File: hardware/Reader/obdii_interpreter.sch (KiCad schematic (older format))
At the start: 0 parts

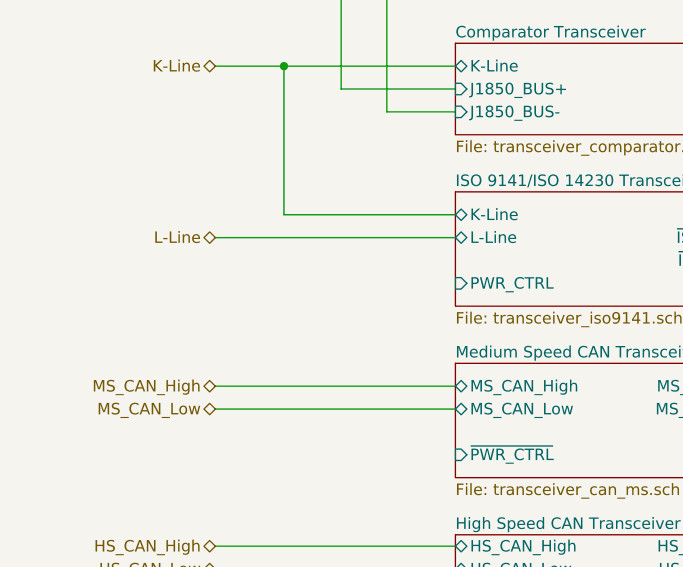
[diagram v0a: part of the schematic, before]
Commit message: Completed Reader schematics for version 0.0.01
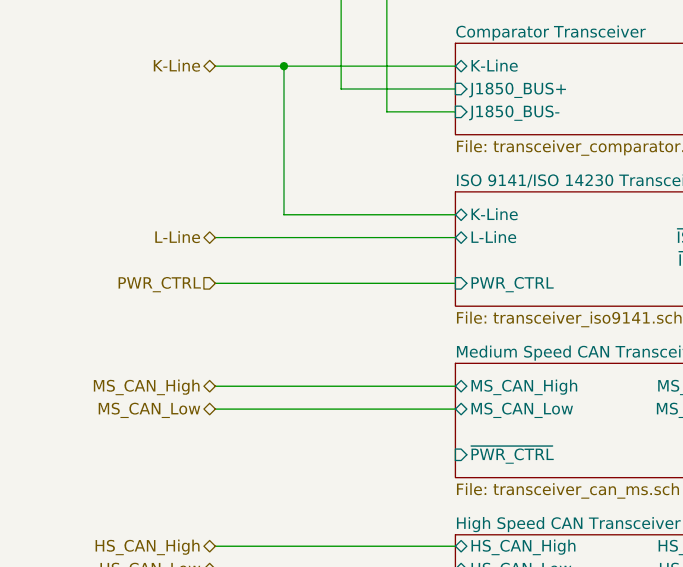
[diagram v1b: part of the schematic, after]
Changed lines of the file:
@@
 $Descr USLetter 11000 8500
 encoding utf-8
-Sheet 9 17
+Sheet 8 18
 Title "CANnect Reader | OBD-II Interpreter"
 Date "2020-10-20"
-Rev "0.0.1"
+Rev "0.0.01"
 Comp "CANtech"
 Comment1 "Created by Choong Jin Ng | jin8383@gmail.com"
@@
 Wire Wire Line
 	4750 6400 1400 6400
+Text HLabel 1400 3450 0    50   Input ~ 0
+PWR_CTRL
+Wire Wire Line
+	1400 3450 2450 3450
 $EndSCHEMATC

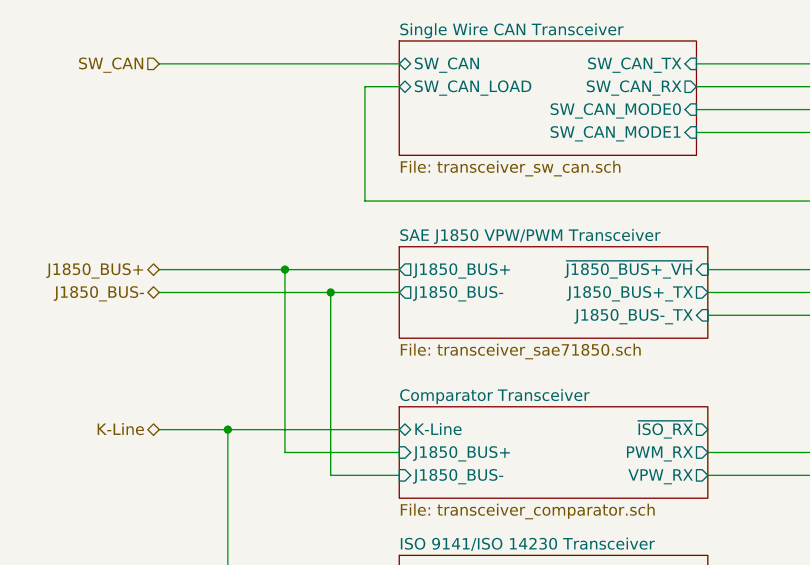
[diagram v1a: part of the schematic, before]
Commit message: Added ESD Protection. Fixed minor bugs on schematic. Attempted placement of components
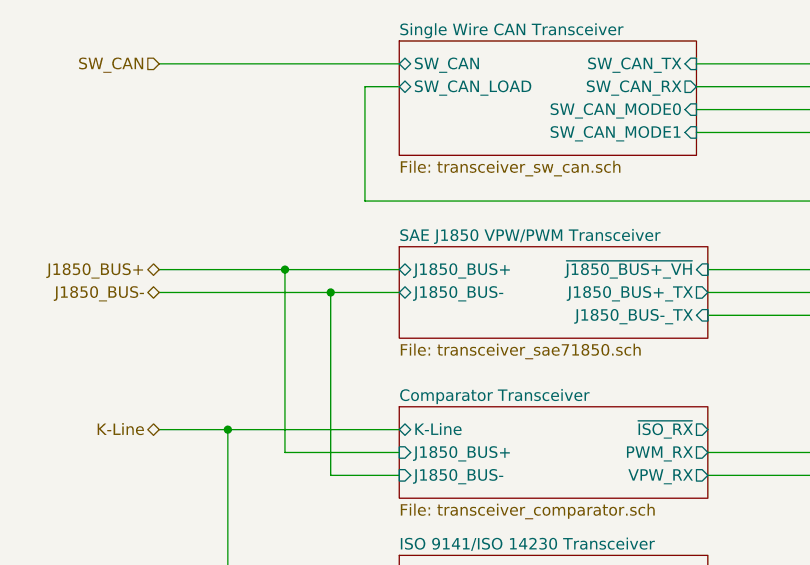
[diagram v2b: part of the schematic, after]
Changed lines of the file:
@@
 $Descr USLetter 11000 8500
 encoding utf-8
-Sheet 8 18
+Sheet 3 19
 Title "CANnect Reader | OBD-II Interpreter"
-Date "2020-10-20"
-Rev "0.0.01"
+Date "2020-10-25"
+Rev "0.0.03"
 Comp "CANtech"
 Comment1 "Created by Choong Jin Ng | jin8383@gmail.com"
@@
 F2 "~J1850_BUS+_VH~" I R 3800 1800 50
 F3 "J1850_BUS+_TX" O R 3800 1900 50
-F4 "J1850_BUS+" O L 2450 1800 50
-F5 "J1850_BUS-_TX" I R 3800 2000 50
-F6 "J1850_BUS-" O L 2450 1900 50
+F4 "J1850_BUS-_TX" I R 3800 2000 50
+F5 "J1850_BUS+" B L 2450 1800 50
+F6 "J1850_BUS-" B L 2450 1900 50
 $EndSheet
 $Sheet
@@
 F7 "SW_CAN_LOAD" B L 2450 1000 50
 $EndSheet
-Text HLabel 1400 5300 0    50   Output ~ 0
-~PWR_CTRL~
 Wire Wire Line
 	1400 900  2450 900
@@
 Wire Wire Line
 	4750 4700 3800 4700
+Wire Wire Line
+	1400 5300 2150 5300
+Wire Wire Line
+	2450 4900 2150 4900
+Wire Wire Line
+	2150 4900 2150 5300
+Wire Wire Line
+	1400 5950 4750 5950
+Wire Wire Line
+	4750 6050 1400 6050
+Text HLabel 1400 5850 0    50   Output ~ 0
+~SLEEP_OBD~
+Wire Wire Line
+	1400 5850 4750 5850
+Wire Wire Line
+	1400 6500 4750 6500
+Text HLabel 1400 6300 0    50   Output ~ 0
+RESET_OBD_SW
+Text HLabel 1400 6400 0    50   Output ~ 0
+~RESET_OBD_HW~
+Wire Wire Line
+	1400 6300 4750 6300
+Wire Wire Line
+	4750 6400 1400 6400
+Text HLabel 1400 3450 0    50   Input ~ 0
+PWR_CTRL
+Wire Wire Line
+	1400 3450 2450 3450
+Connection ~ 2150 5300
+Wire Wire Line
+	2150 5300 4750 5300
 $Sheet
 S 4750 800  1800 5800
@@
 F28 "SW_CAN_MODE0" O L 4750 1100 50
 $EndSheet
-Wire Wire Line
-	1400 5300 2150 5300
-Wire Wire Line
-	2450 4900 2150 4900
-Wire Wire Line
-	2150 4900 2150 5300
-Connection ~ 2150 5300
-Wire Wire Line
-	2150 5300 4750 5300
-Wire Wire Line
-	1400 5950 4750 5950
-Wire Wire Line
-	4750 6050 1400 6050
-Text HLabel 1400 5850 0    50   Output ~ 0
-~SLEEP_OBD~
-Wire Wire Line
-	1400 5850 4750 5850
-Wire Wire Line
-	1400 6500 4750 6500
-Text HLabel 1400 6300 0    50   Output ~ 0
-RESET_OBD_SW
-Text HLabel 1400 6400 0    50   Output ~ 0
-~RESET_OBD_HW~
-Wire Wire Line
-	1400 6300 4750 6300
-Wire Wire Line
-	4750 6400 1400 6400
-Text HLabel 1400 3450 0    50   Input ~ 0
-PWR_CTRL
-Wire Wire Line
-	1400 3450 2450 3450
+Text HLabel 1400 5300 0    50   Output ~ 0
+~PWR_CTRL~
 $EndSCHEMATC

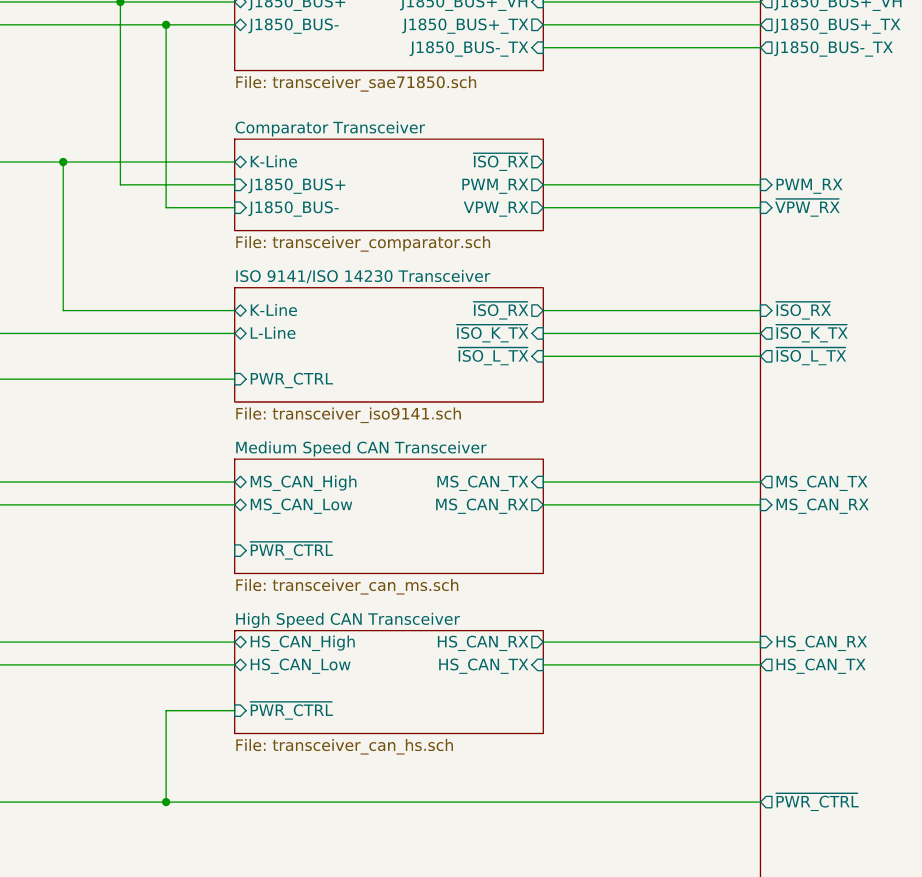
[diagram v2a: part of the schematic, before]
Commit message: Fixed bugs on the reader schematic. Exported Schematic Electrical report
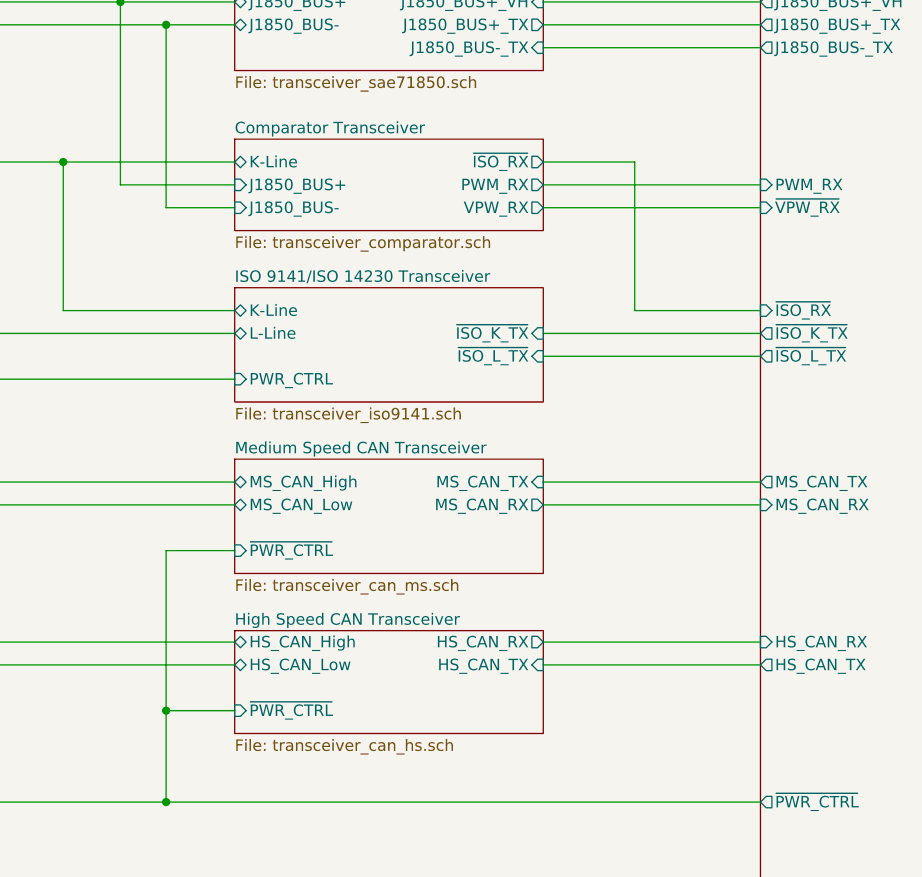
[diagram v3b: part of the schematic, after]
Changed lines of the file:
@@
 F0 "ISO 9141/ISO 14230 Transceiver" 50
 F1 "transceiver_iso9141.sch" 50
-F2 "~ISO_RX~" O R 3800 3150 50
 F3 "~ISO_K_TX~" I R 3800 3250 50
 F4 "PWR_CTRL" I L 2450 3450 50
@@
 Wire Wire Line
 	3800 2000 4750 2000
-Wire Wire Line
-	3800 3150 4750 3150
 Wire Wire Line
 	3800 3250 4750 3250
@@
 Text HLabel 1400 5300 0    50   Output ~ 0
 ~PWR_CTRL~
+Wire Wire Line
+	3800 2500 4200 2500
+Wire Wire Line
+	4200 2500 4200 3150
+Wire Wire Line
+	4200 3150 4750 3150
+Wire Wire Line
+	2150 4900 2150 4200
+Wire Wire Line
+	2150 4200 2450 4200
+Connection ~ 2150 4900
 $EndSCHEMATC

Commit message: Revising reader
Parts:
- added J_OBD_1: 1546931-2, footprints:1546931-2, symbol 1546931-2:1546931-2
- added J_OBD_2: 4157, Connector_PinSocket_2.54mm:PinSocket_1x20_P2.54mm_Vertical, symbol CANtech:4157
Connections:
- net Comparator Transceiver/PWM_RX: now also J_OBD_2.12 (Pin_12)
- net Comparator Transceiver/VPW_RX: now also J_OBD_2.11 (Pin_11)
- net Comparator Transceiver/~ISO_RX~: now also J_OBD_2.6 (Pin_6)
- net High Speed CAN Transceiver/HS_CAN_RX: now also J_OBD_2.10 (Pin_10)
- net High Speed CAN Transceiver/HS_CAN_TX: now also J_OBD_2.9 (Pin_9)
- net ISO 9141/ISO 14230 Transceiver/~ISO_K_TX~: now also J_OBD_2.4 (Pin_4)
- net ISO 9141/ISO 14230 Transceiver/~ISO_L_TX~: now also J_OBD_2.2 (Pin_2)
- net OBDII Chip/J1850_BUS+_TX: now also J_OBD_2.5 (Pin_5)
- net OBDII Chip/J1850_BUS-_TX: now also J_OBD_2.3 (Pin_3)
- net OBDII Chip/STATUS_LED: now also J_OBD_2.20 (Pin_20)
- net OBDII Chip/SW_CAN_LOAD: now also J_OBD_2.14 (Pin_14)
- net OBDII Chip/SW_CAN_MODE0: now also J_OBD_2.17 (Pin_17)
- net OBDII Chip/SW_CAN_MODE1: now also J_OBD_2.13 (Pin_13)
- net OBDII Chip/SW_CAN_RX: now also J_OBD_2.15 (Pin_15)
- net OBDII Chip/SW_CAN_TX: now also J_OBD_2.16 (Pin_16)
- net OBDII Chip/~HOST_ACT_LED~: now also J_OBD_2.19 (Pin_19)
- net OBDII Chip/~J1850_BUS+_VH~: now also J_OBD_2.1 (Pin_1)
- net OBDII Chip/~OBD_ACT_LED~: now also J_OBD_2.18 (Pin_18)
- net RESET_OBD_SW: now also J_OBD_1.1
- net ~RESET_OBD_HW~: now also J_OBD_1.2
- new net OBDII Chip/MS_CAN_RX: J_OBD_2.7 (Pin_7)
- new net OBDII Chip/MS_CAN_TX: J_OBD_2.8 (Pin_8)
- no-connect marks 3 -> 13
